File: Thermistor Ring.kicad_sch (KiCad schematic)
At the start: 18 parts, among them J1 Conn_01x04_Socket, U1 TPS7A2018PDBVR, U2 MCP9808T-E/MC, U3 MCP9808T-E/MC, U4 MCP9808T-E/MC, U5 MCP9808T-E/MC, U6 MCP9808T-E/MC, U7 MCP9808T-E/MC

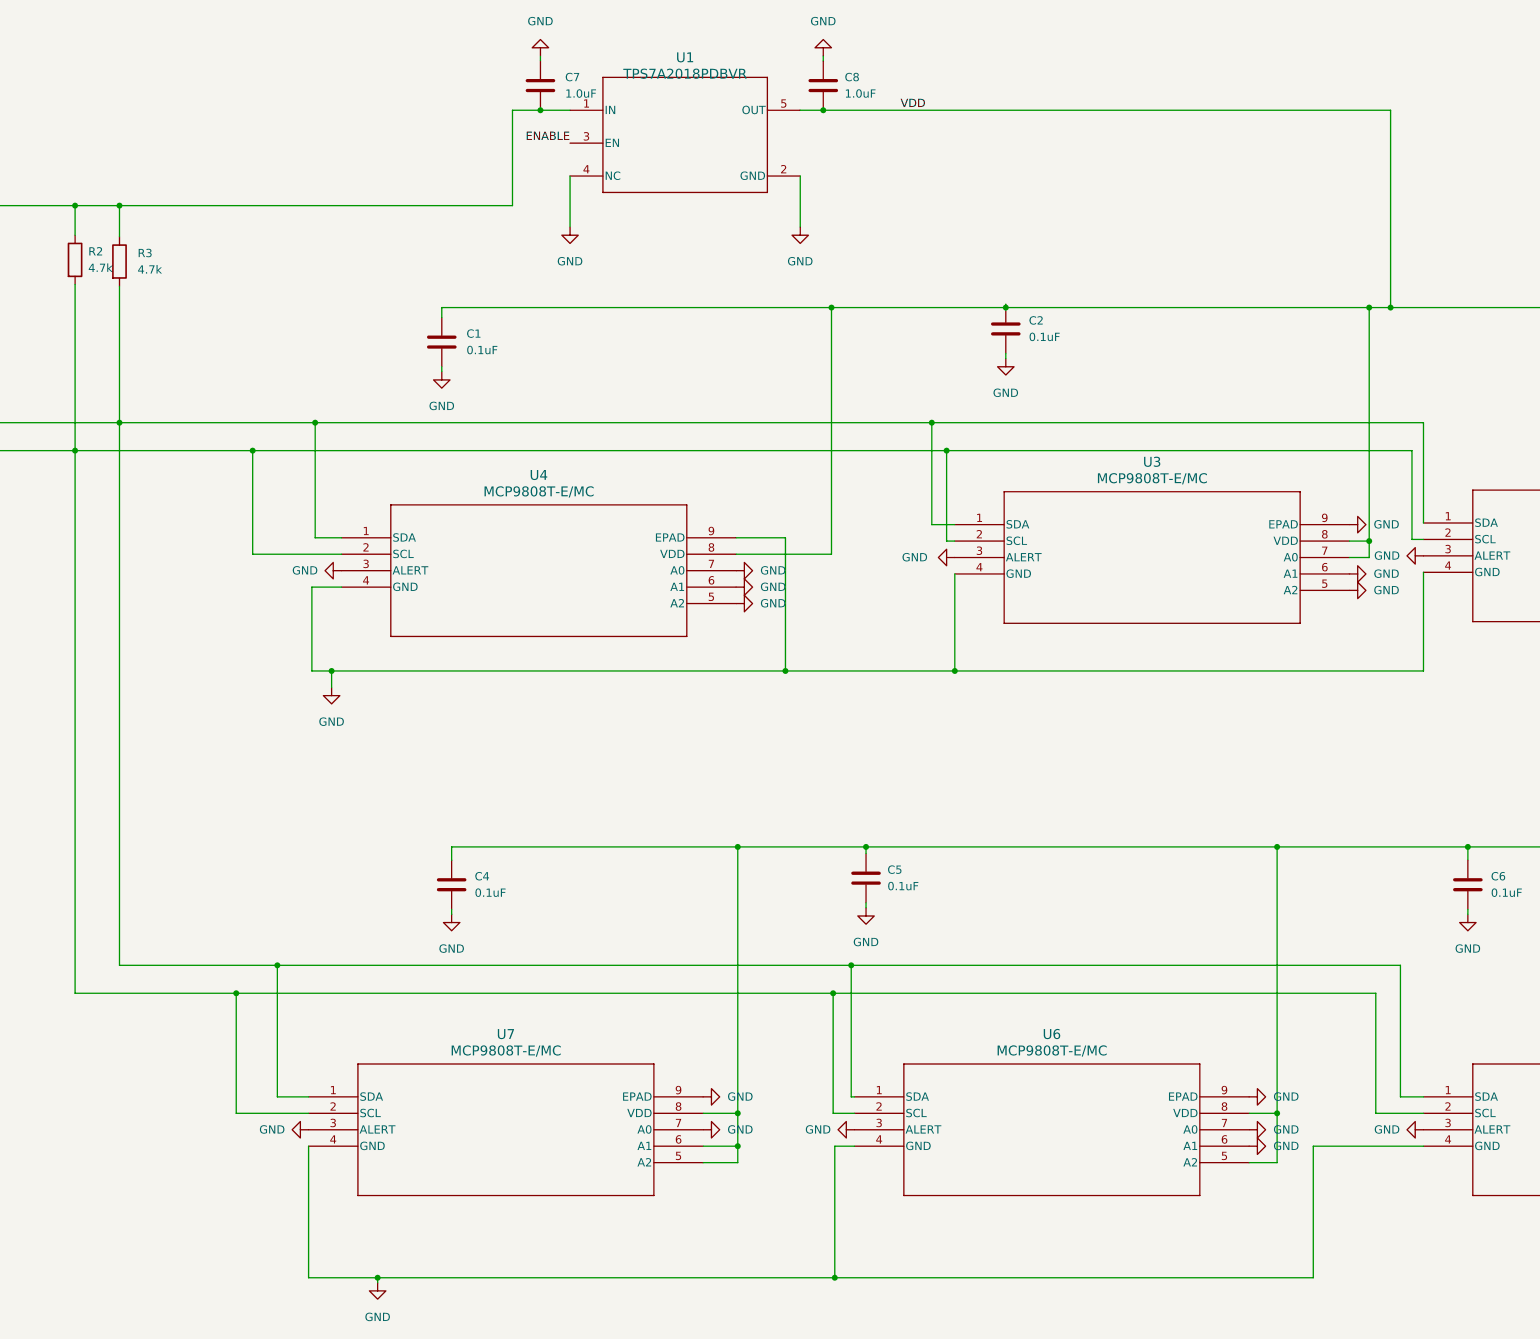
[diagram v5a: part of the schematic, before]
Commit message: Pass DRC and fix fills
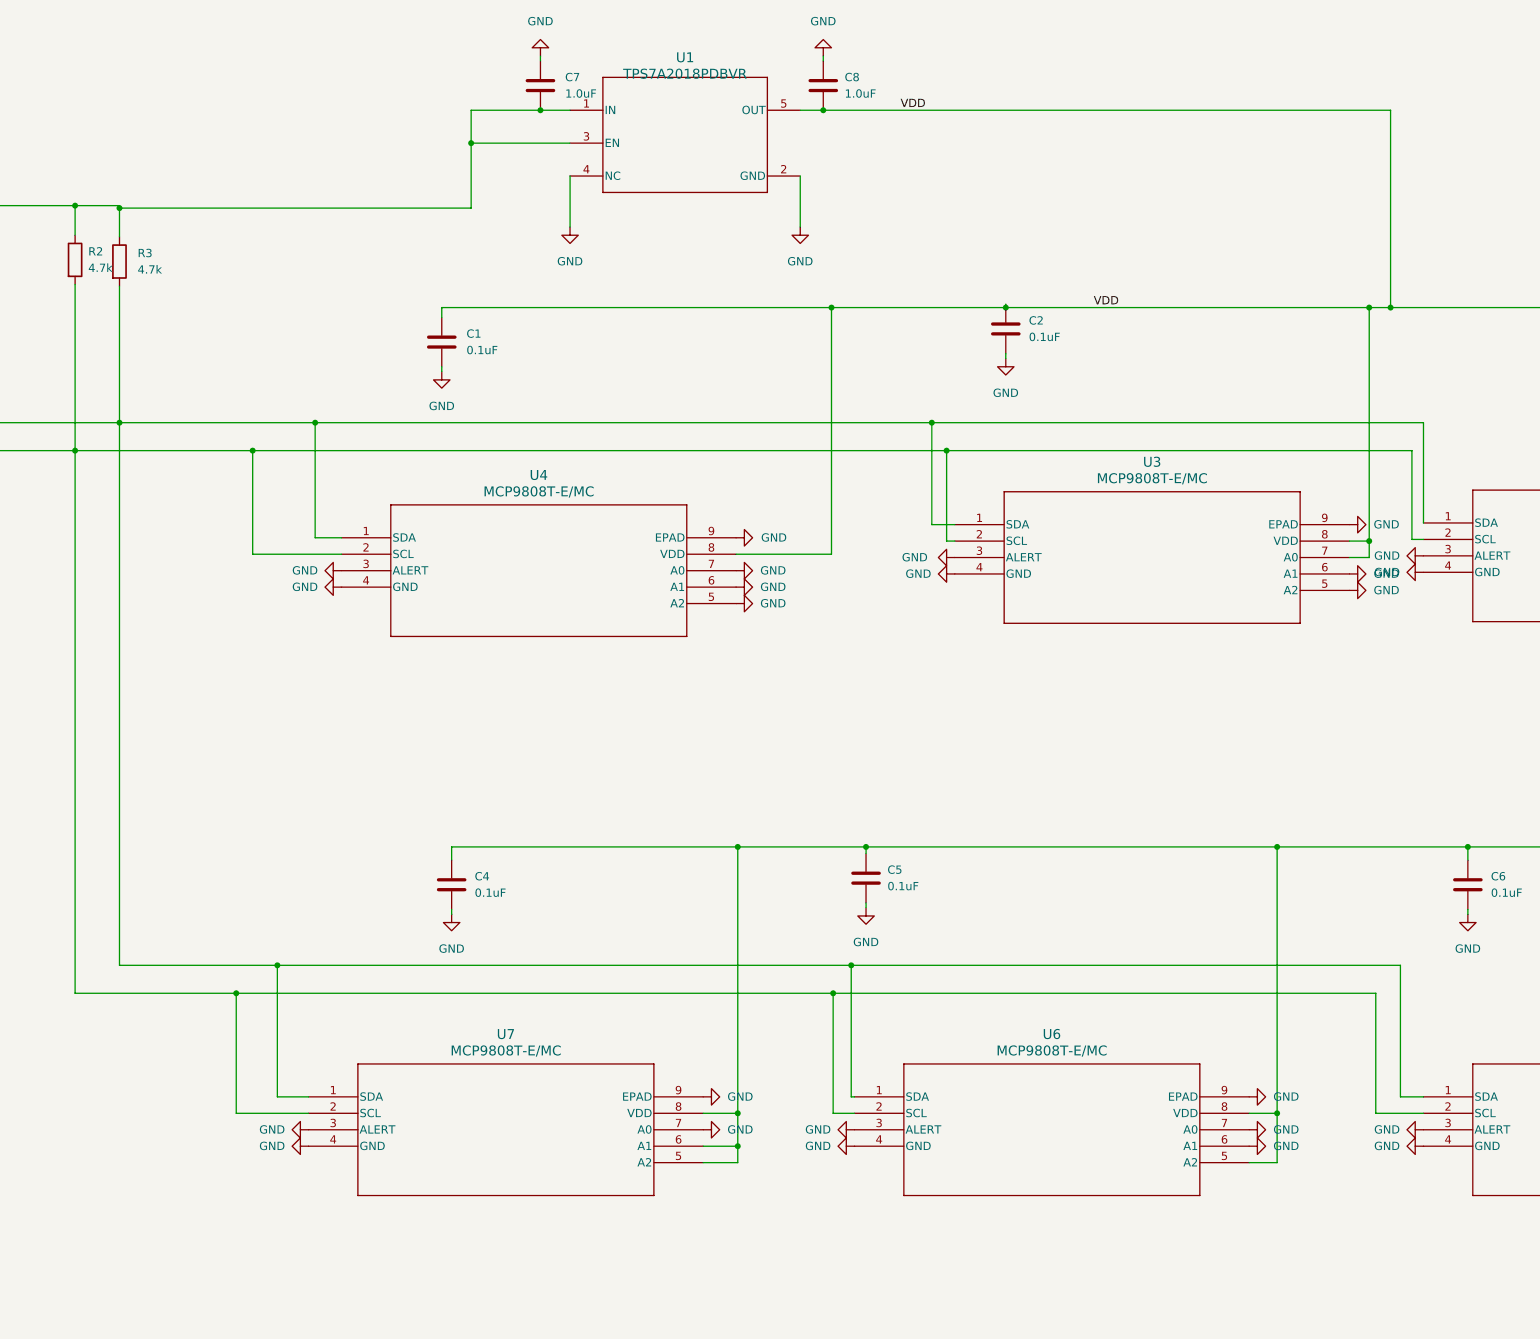
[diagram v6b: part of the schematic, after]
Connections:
- net ENABLE is gone; now on net Power 3.3-5V: U1.3 (EN)

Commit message: Reduce size of epad, improve layout
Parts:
- C1, C2, C3, C4, R2, R3, U1, U2, U3, U4, U5, U6, U7: OnHand (none) -> No
- C5, C6, C7, C8, J1: OnHand (none) -> Yes
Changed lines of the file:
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@@
+      (effects (font (size 1.27 1.27)) hide)
+    )
+    (property "OnHand" "Yes" (at 200.2304 39.3864 0)
       (effects (font (size 1.27 1.27)) hide)
     )
@@
       (effects (font (size 1.27 1.27)) hide)
     )
+    (property "OnHand" "Yes" (at 35.6384 99.0764 0)
+      (effects (font (size 1.27 1.27)) hide)
+    )
     (pin "1")
     (pin "4")
@@
       (effects (font (size 1.27 1.27)) hide)
     )
+    (property "OnHand" "Yes" (at 206.8344 161.8144 0)
+      (effects (font (size 1.27 1.27)) hide)
+    )
     (pin "2")
     (pin "1")
@@
       (effects (font (size 1.27 1.27)) hide)
     )
+    (property "OnHand" "No" (at 228.4244 76.9784 0)
+      (effects (font (size 1.27 1.27)) hide)
+    )
     (pin "2")
     (pin "1")
@@
       (effects (font (size 1.27 1.27)) hide)
     )
+    (property "OnHand" "No" (at 326.2144 77.9944 0)
+      (effects (font (size 1.27 1.27)) hide)
+    )
     (pin "2")
     (pin "1")
@@
     )
     (property "Datasheet" "~" (at 142.8264 162.8304 0)
+      (effects (font (size 1.27 1.27)) hide)
+    )
+    (property "OnHand" "No" (at 142.8264 162.8304 0)
       (effects (font (size 1.27 1.27)) hide)
     )
@@
       (effects (font (size 1.27 1.27)) hide)
     )
+    (property "OnHand" "Yes" (at 156.5424 39.3864 0)
+      (effects (font (size 1.27 1.27)) hide)
+    )
     (pin "2")
     (pin "1")
@@
     )
     (property "Datasheet" "~" (at 84.6604 66.3104 0)
+      (effects (font (size 1.27 1.27)) hide)
+    )
+    (property "OnHand" "No" (at 84.6604 66.3104 0)
       (effects (font (size 1.27 1.27)) hide)
     )
@@
     (property "Datasheet" "MCP9808T-E/MC" (at 125.8084 109.2364 0)
       (effects (font (size 1.27 1.27) italic) hide)
+    )
+    (property "OnHand" "No" (at 125.8084 109.2364 0)
+      (effects (font (size 1.27 1.27)) hide)
     )
     (pin "1")
@@
       (effects (font (size 1.27 1.27) italic) hide)
     )
+    (property "OnHand" "No" (at 292.9404 195.5964 0)
+      (effects (font (size 1.27 1.27)) hide)
+    )
     (pin "1")
     (pin "2")
@@
       (effects (font (size 1.27 1.27) italic) hide)
     )
+    (property "OnHand" "No" (at 220.5504 107.2044 0)
+      (effects (font (size 1.27 1.27)) hide)
+    )
     (pin "1")
     (pin "2")
@@
       (effects (font (size 1.27 1.27) italic) hide)
     )
+    (property "OnHand" "No" (at 292.9404 106.9504 0)
+      (effects (font (size 1.27 1.27)) hide)
+    )
     (pin "1")
     (pin "2")
@@
       (effects (font (size 1.27 1.27)) hide)
     )
+    (property "OnHand" "No" (at 141.3024 79.0104 0)
+      (effects (font (size 1.27 1.27)) hide)
+    )
     (pin "2")
     (pin "1")
@@
     (property "Datasheet" "MCP9808T-E/MC" (at 120.7284 195.5964 0)
       (effects (font (size 1.27 1.27) italic) hide)
+    )
+    (property "OnHand" "No" (at 120.7284 195.5964 0)
+      (effects (font (size 1.27 1.27)) hide)
     )
     (pin "1")
@@
       (effects (font (size 1.27 1.27) italic) hide)
     )
+    (property "OnHand" "No" (at 161.1144 43.1964 0)
+      (effects (font (size 1.27 1.27)) hide)
+    )
     (pin "4")
     (pin "5")
@@
     (property "Datasheet" "MCP9808T-E/MC" (at 205.0564 195.5964 0)
       (effects (font (size 1.27 1.27) italic) hide)
+    )
+    (property "OnHand" "No" (at 205.0564 195.5964 0)
+      (effects (font (size 1.27 1.27)) hide)
     )
     (pin "1")
@@
       (effects (font (size 1.27 1.27)) hide)
     )
+    (property "OnHand" "No" (at 91.5184 66.5644 0)
+      (effects (font (size 1.27 1.27)) hide)
+    )
     (pin "1")
     (pin "2")
@@
       (effects (font (size 1.27 1.27)) hide)
     )
+    (property "OnHand" "Yes" (at 299.7984 162.8304 0)
+      (effects (font (size 1.27 1.27)) hide)
+    )

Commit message: Change to MSOP thermistor
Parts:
- removed C7, C8: 1.0uF, Capacitor_SMD:C_0603_1608Metric, symbol Device:C
- removed U1: TPS7A2018PDBVR, TPS7A2018PDBVR:DBV0005A-IPC_A, symbol TI_LDO_ TPS7A2018PDBVR:TPS7A2018PDBVR
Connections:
- net VDD is gone; now on net Power 3.3-5V: C1.1, C2.1, C3.1, C4.1, C5.1, C6.1, U2.6 (A1), U2.8 (VDD), U3.7 (A0), U3.8 (VDD), U4.8 (VDD), U5.5 (A2), U5.7 (A0), U5.8 (VDD), U6.5 (A2), U6.8 (VDD), U7.5 (A2), U7.6 (A1), U7.8 (VDD)
- net GND: no longer U2.3 (ALERT), U3.3 (ALERT), U4.3 (ALERT), U5.3 (ALERT), U6.3 (ALERT), U7.3 (ALERT)
